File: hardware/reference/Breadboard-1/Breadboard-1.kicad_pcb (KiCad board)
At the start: 2 copper layers, 50.8 x 69.9 mm, 57 parts, among them J1 Left, J2 Right, J3 ICSP, Q31 HSM0903, Q32 HSM0903, Q41 FDG1024NZ, Q42 FDG1024NZ, Q43 FDG1024NZ, U11 AMS1117-5.0, U21 PIC18F25K50-xML

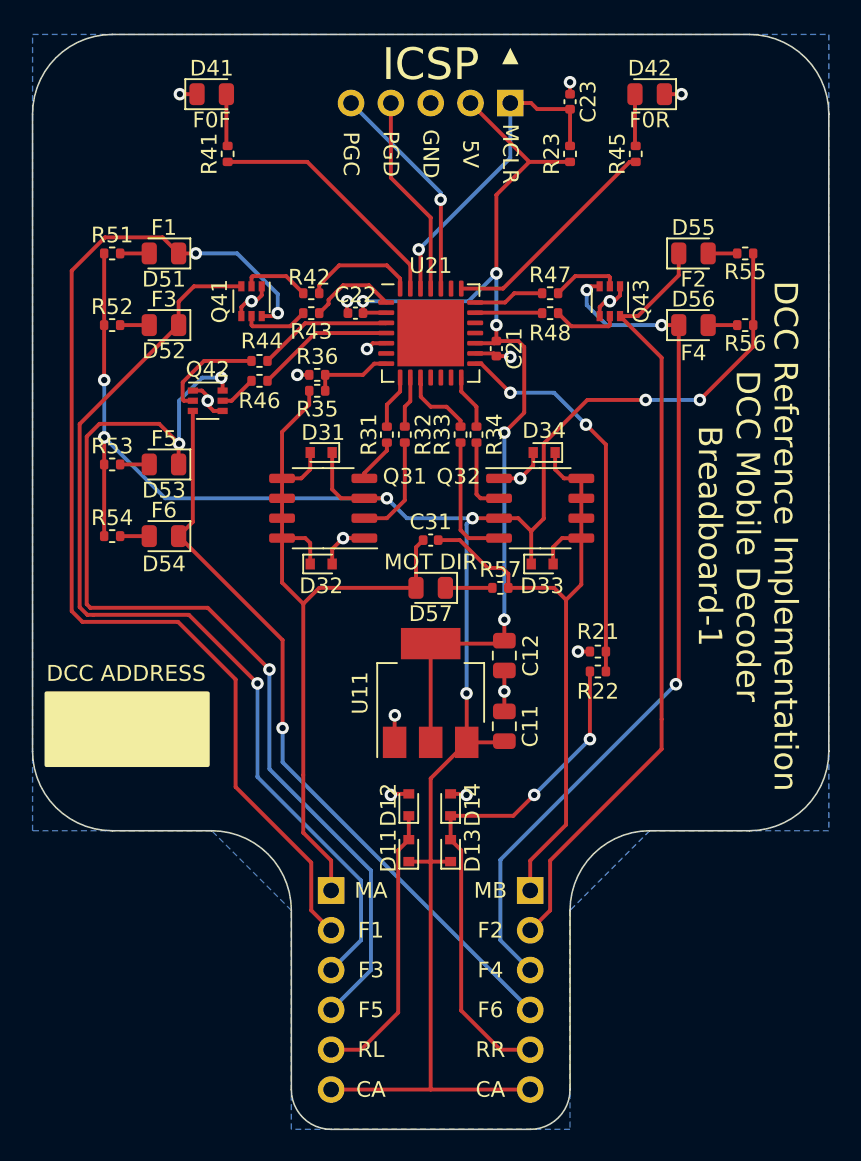
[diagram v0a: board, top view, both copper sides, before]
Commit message: Added V3V3USB capacitor and USB Micro-B port for debugging.
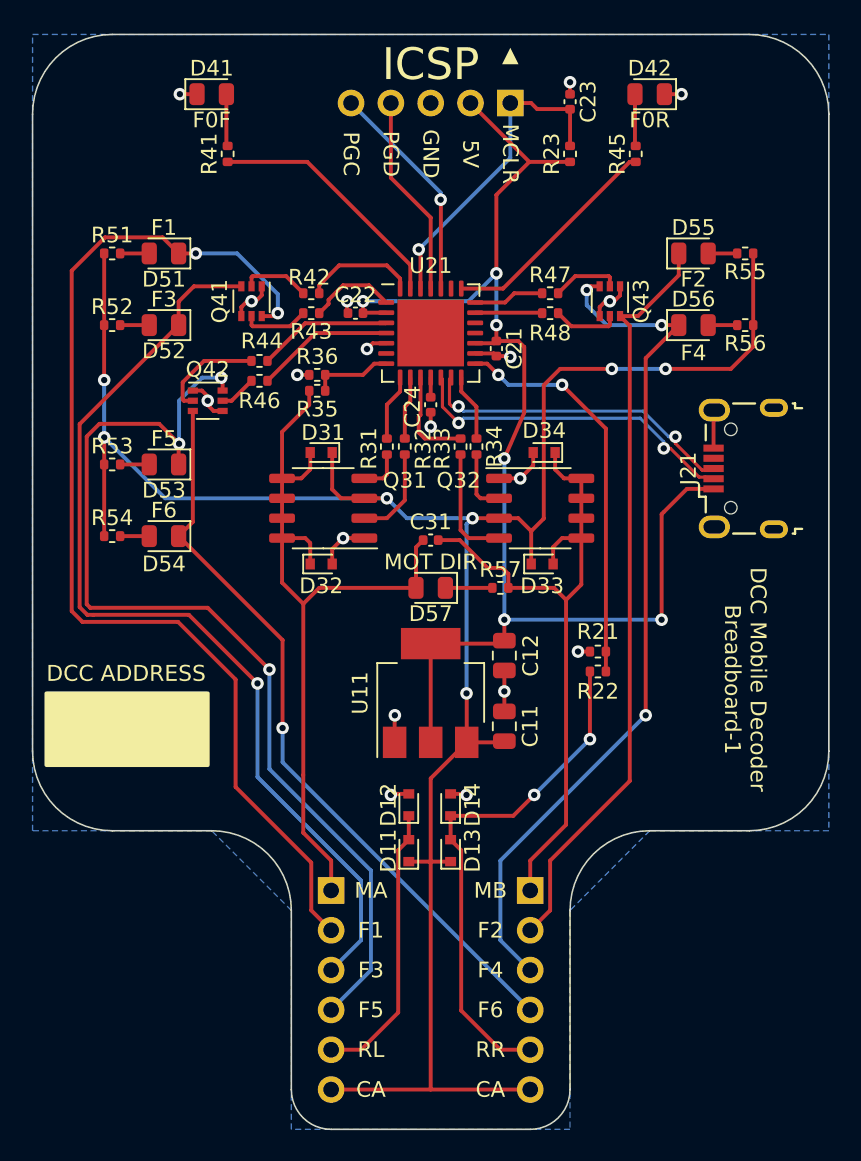
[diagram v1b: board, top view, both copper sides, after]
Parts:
- added C24: 47nf, Capacitor_SMD:C_0402_1005Metric, F.Cu at (76.2, 74.4)
- added J21: USB_B_Micro, Connector_USB:USB_Micro-B_Wuerth_629105150521, F.Cu at (96.1, 78.5)
- Q41, Q42, Q43: value FDG1024NZ -> 2N7002
- R21, R36: value 1K -> 1K3
- R22: value 5K -> 6K6
- R34: value 200 -> 220
- R35: value 2K -> 6K6
- moved R31 0.76 mm to (73.4, 77.1)
- moved R32 0.76 mm to (74.5, 77.1)
- moved R33 0.76 mm to (78.1, 77.1)
- moved R34 0.76 mm to (79.1, 77.1)
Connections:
- U21 pad 11: unconnected-(U21-Pad11) -> Net-(C24-Pad2)
- U21 pad 12: unconnected-(U21-Pad12) -> /D-
- U21 pad 13: unconnected-(U21-Pad13) -> /D+
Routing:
- net /D-: track 0.00 -> 21.6 mm, vias 0 -> 2
- net /D+: track 0.00 -> 20.6 mm, vias 0 -> 2
- net +5V: track 65.4 -> 85.9 mm, vias 5 -> 6
- net GND: track 30.5 -> 33.8 mm, vias 17 -> 18
- net Vdrive: track 139.0 -> 141.2 mm
- net F2_SP: track 50.0 -> 48.3 mm
- net P1C: track 4.78 -> 6.38 mm
- net Net-(C24-Pad2): track 0.00 -> 1.25 mm
- net P1D: track 3.53 -> 4.29 mm
- net P1A: track 3.48 -> 4.24 mm
- net Net-(Q32-Pad4): track 8.25 -> 7.49 mm
- net Net-(Q32-Pad2): track 4.84 -> 4.08 mm
- net Net-(Q31-Pad2): track 6.74 -> 5.98 mm
- net P1B: track 3.27 -> 4.03 mm
- net Net-(R21-Pad1): track 25.0 -> 25.6 mm
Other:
- board text added: "DCC Mobile Decoder Breadboard-1"
- board text removed: "DCC Reference Implementation DCC Mobile Decoder Breadboard-1"

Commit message: Move USB to the External Connectivity section.
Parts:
- renumbered J21 to J4
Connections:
- net /D+ renamed D+
- net /D- renamed D-
- C24 pad 1: GND -> Net-(C24-Pad1)
- C24 pad 2: Net-(C24-Pad2) -> GND
- U21 pad 11: Net-(C24-Pad2) -> Net-(C24-Pad1)
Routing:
- net Net-(C24-Pad2): track 1.25 -> 0.00 mm
- net Net-(C24-Pad1): track 0.00 -> 0.92 mm

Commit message: Make functions symmetrical.
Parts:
- moved R54 41.3 mm to (96.3, 74.2), turned to 180 degrees
- moved D54 34.9 mm to (93.0, 74.2), turned to 0 degrees
- moved J4 4.50 mm to (97.8, 82.7)
- moved D53 4.32 mm to (59.2, 73.9)
- moved R53 4.32 mm to (55.9, 73.9)
- moved Q42 2.01 mm to (63.1, 75.9)
- moved R44 0.51 mm to (65.8, 71.6)
- moved R46 0.51 mm to (65.8, 72.9)
- turned C24 to -90 degrees
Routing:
- net F6_SP: track 47.9 -> 155.1 mm, vias 1 -> 3
- net F5_SP: track 64.5 -> 61.0 mm
- net D+: track 20.6 -> 24.1 mm
- net D-: track 21.6 -> 25.1 mm
- net +5V: track 85.9 -> 83.3 mm
- net F3_SP: track 61.7 -> 63.7 mm
- net Net-(Q42-Pad5): track 2.37 -> 3.83 mm
- net RAIL_R: track 33.4 -> 32.0 mm
- net Vdrive: track 141.2 -> 140.1 mm
- net GND: track 34.2 -> 33.3 mm
- net Net-(Q42-Pad2): track 6.74 -> 7.61 mm
- net F4_SP: track 54.9 -> 54.3 mm
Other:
- board text added: "COMMON ANODE"
- board text added: "USB"
- board text removed: "CA"

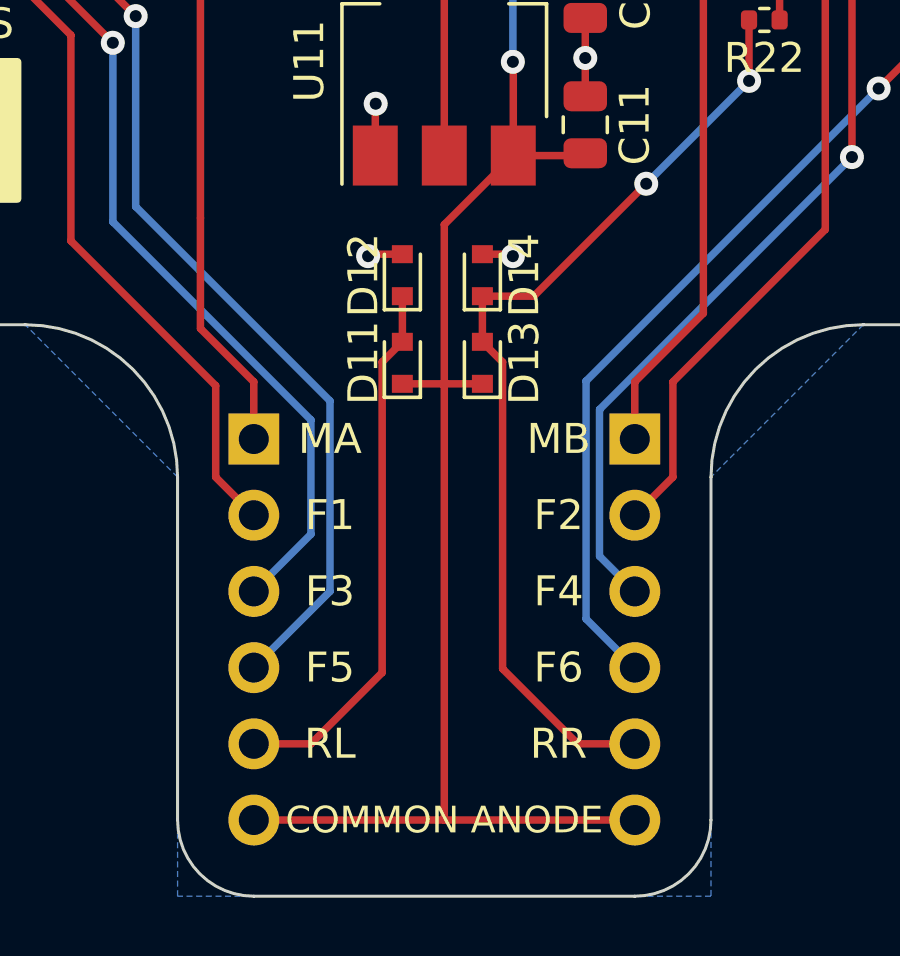
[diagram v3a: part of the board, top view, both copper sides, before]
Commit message: Moved to SOD-123 diodes for cheaper, better rating parts.
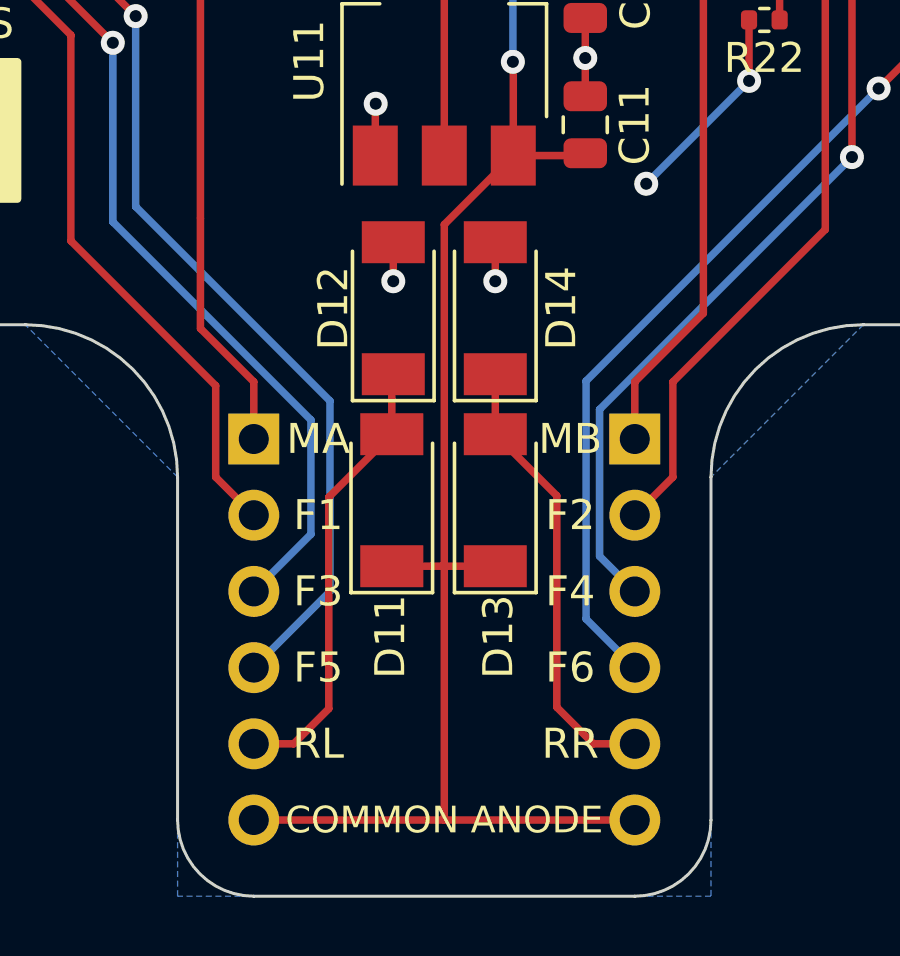
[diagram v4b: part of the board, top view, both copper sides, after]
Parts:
- D11, D12, D13, D14: footprint Diode_SMD:D_SOD-523 -> Diode_SMD:D_SOD-128
- moved D13 4.60 mm to (77.9, 107.5)
- moved D11 4.59 mm to (74.5, 107.5)
- moved D14 1.18 mm to (77.9, 101.0)
- moved D12 1.14 mm to (74.5, 101.0)
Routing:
- net RAIL_R: track 32.0 -> 21.9 mm
- net RAIL_L: track 18.1 -> 15.0 mm
- net Vdrive: track 140.1 -> 140.9 mm

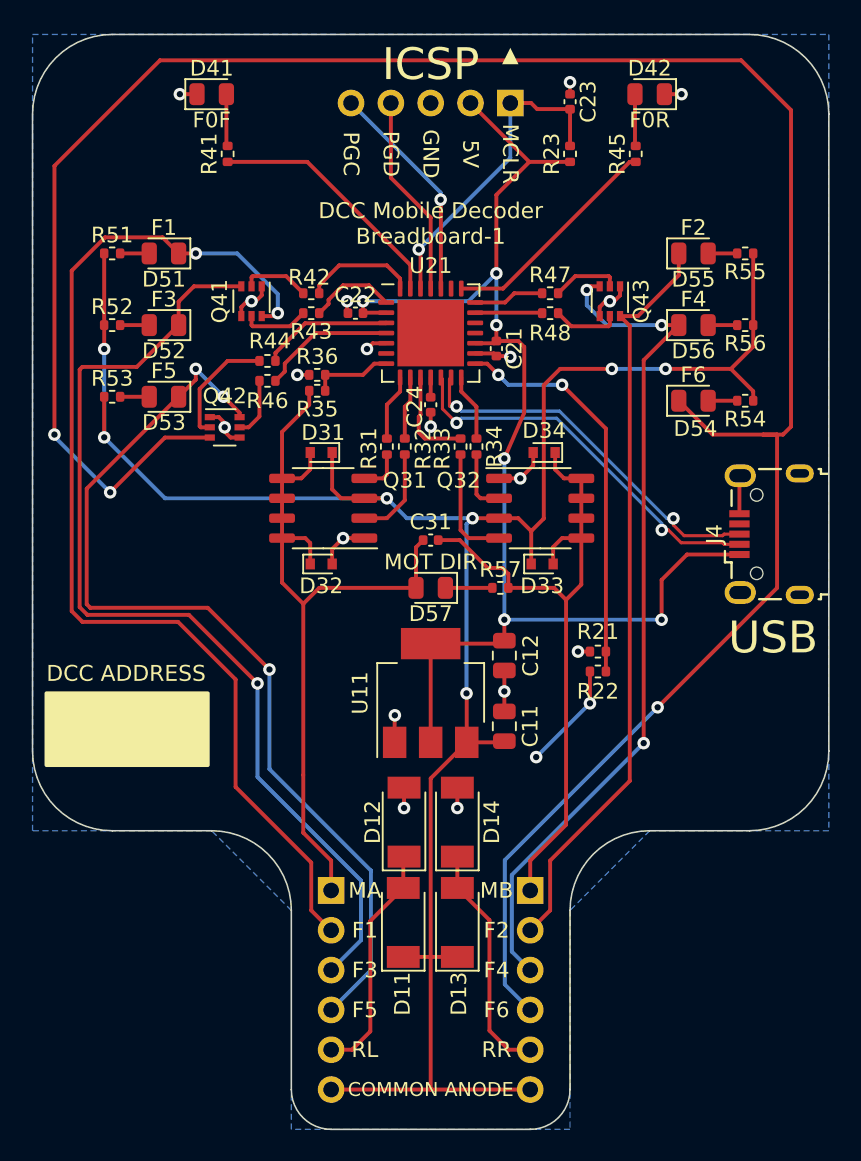
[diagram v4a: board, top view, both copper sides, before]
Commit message: Chip selection update, new symbols, improved reference design.
Updated the chip selection document based on availability.

Added new symbols for the chips in the chip selection document.

Switched the reference design to an SSOP-20 package and improved the
layout in general.
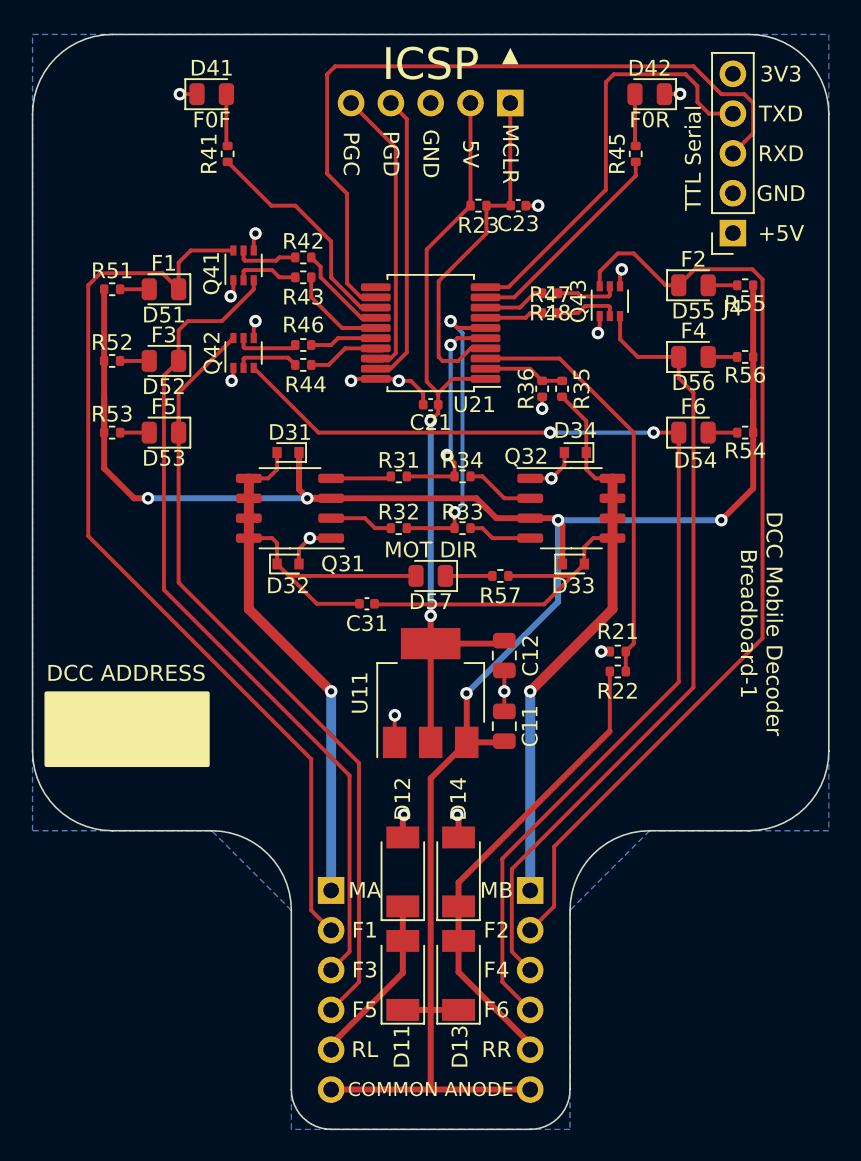
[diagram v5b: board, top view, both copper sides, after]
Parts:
- removed C22: 100nF, Capacitor_SMD:C_0402_1005Metric
- removed C24: 47nf, Capacitor_SMD:C_0402_1005Metric
- J4: value USB_B_Micro -> TTL Serial; footprint Connector_USB:USB_Micro-B_Wuerth_629105150521 -> Connector_PinSocket_2.54mm:PinSocket_1x05_P2.54mm_Vertical
- U21: value PIC18F25K50-xML -> PIC18F06Q40-x/SS; footprint Package_DFN_QFN:QFN-28-1EP_6x6mm_P0.65mm_EP4.25x4.25mm -> Package_SO:SSOP-20_5.3x7.2mm_P0.65mm
- moved J4 19.3 mm to (95.5, 63.5), turned to 180 degrees
- moved R35 15.6 mm to (84.6, 73.4), turned to -90 degrees
- moved R36 14.4 mm to (83.3, 73.4), turned to 90 degrees
- moved C23 7.41 mm to (81.8, 61.7), turned to 180 degrees
- moved R23 6.71 mm to (79.2, 61.7), turned to 0 degrees
- moved C31 5.75 mm to (72.1, 87.1)
- moved C21 5.51 mm to (76.2, 74.4), turned to 0 degrees
- moved R32 5.22 mm to (74.2, 82.3), turned to 180 degrees
- moved R33 5.21 mm to (78.2, 82.3), turned to 180 degrees
- moved Q42 4.89 mm to (64.3, 71.1), turned to 90 degrees
- moved R43 3.59 mm to (68.1, 65.0)
- moved D13 3.38 mm to (78.0, 110.8)
- moved D11 3.38 mm to (74.4, 110.8)
- moved R46 3.23 mm to (68.1, 70.6)
- moved D12 3.18 mm to (74.4, 104.2)
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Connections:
- J4 pad 1: +5V -> unconnected-(J4-Pad1)
- J4 pad 2: D- -> GND
- J4 pad 3: D+ -> RXD
- J4 pad 4: unconnected-(J4-Pad4) -> TXD
- J4 pad 5: GND -> unconnected-(J4-Pad5)
- R33 pad 2: P1C -> P1B
- R34 pad 2: P1D -> P1A
- R35 pad 2: MOT_A -> MOT_B
- R43 pad 1: F2 -> F3
- R44 pad 1: F3 -> F5
- R46 pad 1: F4 -> F6
- R47 pad 1: F5 -> F2
- R48 pad 1: F6 -> F4
- U21 pad 1: F2 -> +5V
- U21 pad 10: P1C -> TXD
- U21 pad 11: Net-(C24-Pad1) -> unconnected-(U21-Pad11)
- U21 pad 12: D- -> RXD
- U21 pad 13: D+ -> F0F
- U21 pad 14: P1D -> F3
- U21 pad 15: Net-(R21-Pad1) -> F1
- U21 pad 16: GND -> F6
- U21 pad 17: +5V -> F5
- U21 pad 18: unconnected-(U21-Pad18) -> PGC
- U21 pad 19: unconnected-(U21-Pad19) -> PGD
- U21 pad 2: +5V -> BackEMF
- U21 pad 20: F6 -> GND
- U21 pad 3: F3 -> Net-(R21-Pad1)
- U21 pad 4: F4 -> MCLR
- U21 pad 5: GND -> P1A
- U21 pad 6: unconnected-(U21-Pad6) -> P1B
- U21 pad 7: BackEMF -> F2
- U21 pad 8: P1A -> F4
- U21 pad 9: P1B -> F0R
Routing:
- net F6_SP: track 155.1 -> 73.1 mm, vias 3 -> 2
- net RXD: track 0.00 -> 48.2 mm
- net +5V: track 83.3 -> 50.6 mm, vias 6 -> 2
- net TXD: track 0.00 -> 27.1 mm
- net D-: track 25.1 -> 0.00 mm, vias 2 -> 0
- net D+: track 24.1 -> 0.00 mm, vias 2 -> 0
- net P1B: track 4.03 -> 19.4 mm, vias 0 -> 2
- net MOT_B: track 44.0 -> 57.1 mm, vias 0 -> 1
- net F2_SP: track 48.3 -> 61.0 mm
- net F3_SP: track 63.7 -> 53.0 mm, vias 1 -> 0
- net F1_SP: track 70.4 -> 59.9 mm, vias 2 -> 0
- net F5_SP: track 61.0 -> 50.7 mm, vias 3 -> 0
- net P1A: track 4.24 -> 14.1 mm, vias 0 -> 2
- net RAIL_R: track 21.9 -> 30.0 mm, vias 2 -> 0
- net P1C: track 6.38 -> 0.00 mm
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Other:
- board text added: "+5V"
- board text added: "3V3"
- board text added: "RXD"
- board text added: "TXD"
- board text removed: "USB"

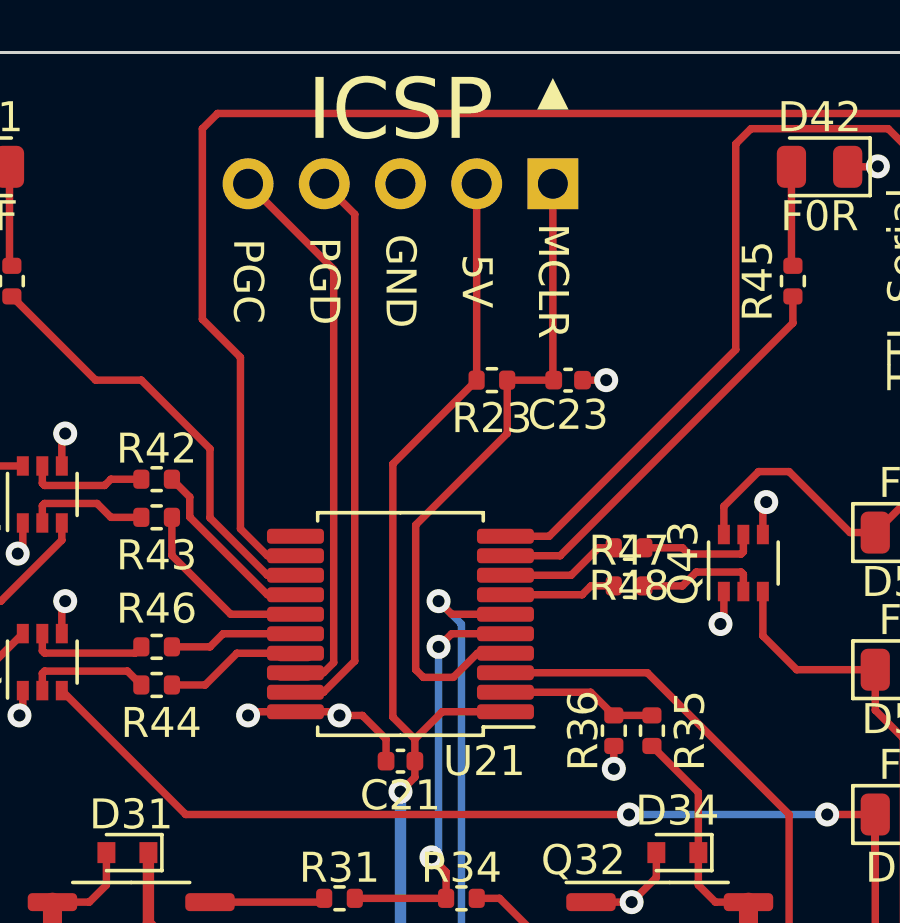
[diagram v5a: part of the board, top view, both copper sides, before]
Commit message: Updated to the new processor and lots of board layout cleanup.
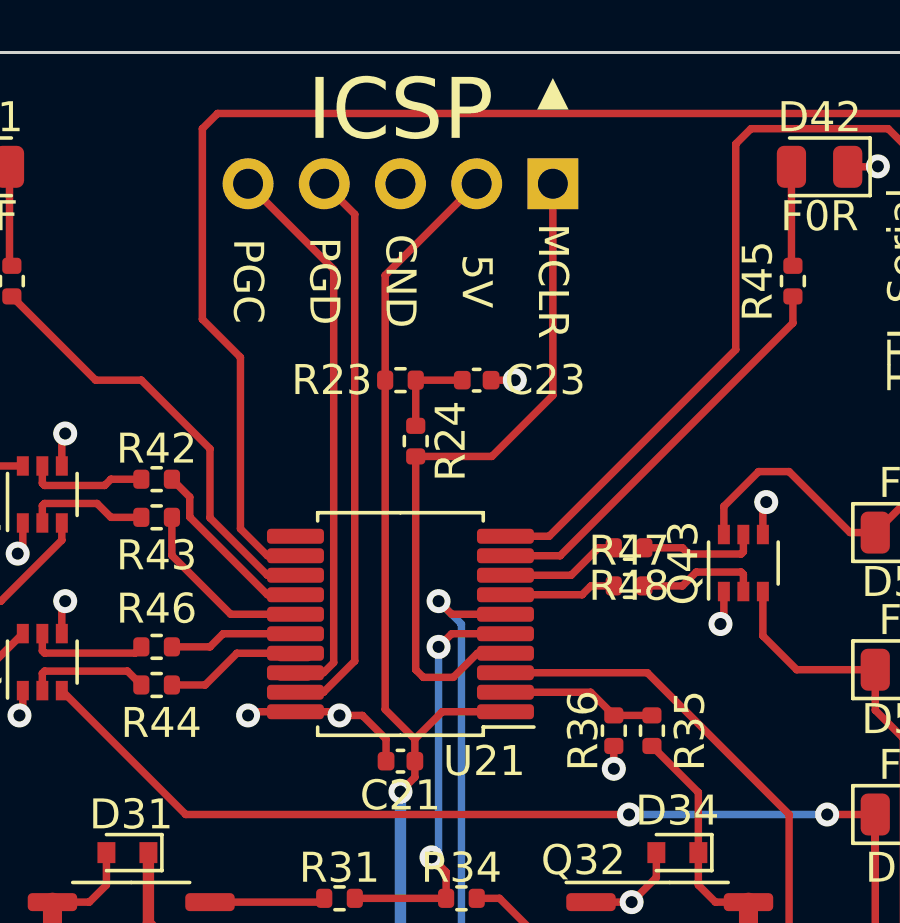
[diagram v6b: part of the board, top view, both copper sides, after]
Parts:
- added R24: 220, Resistor_SMD:R_0402_1005Metric, F.Cu at (76.7, 63.8)
- moved C23 3.05 mm to (78.7, 61.7)
- moved R23 3.05 mm to (76.2, 61.7)
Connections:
- C23 pad 2: MCLR -> Net-(C23-Pad2)
- R23 pad 2: MCLR -> Net-(C23-Pad2)
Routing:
- net Net-(C23-Pad2): track 0.00 -> 3.07 mm
- net MCLR: track 23.6 -> 24.1 mm
